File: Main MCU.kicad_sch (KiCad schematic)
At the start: 53 parts, among them J1 F407 SWD, J2 GPIO, J3 Conn_01x02_Pin, SW1 SW_Push, SW2 SW_Push, SW3 SW_Push, SW4 SW_Push, U1 STM32F407VGTx, U2 MCP1825S-3302E/EB

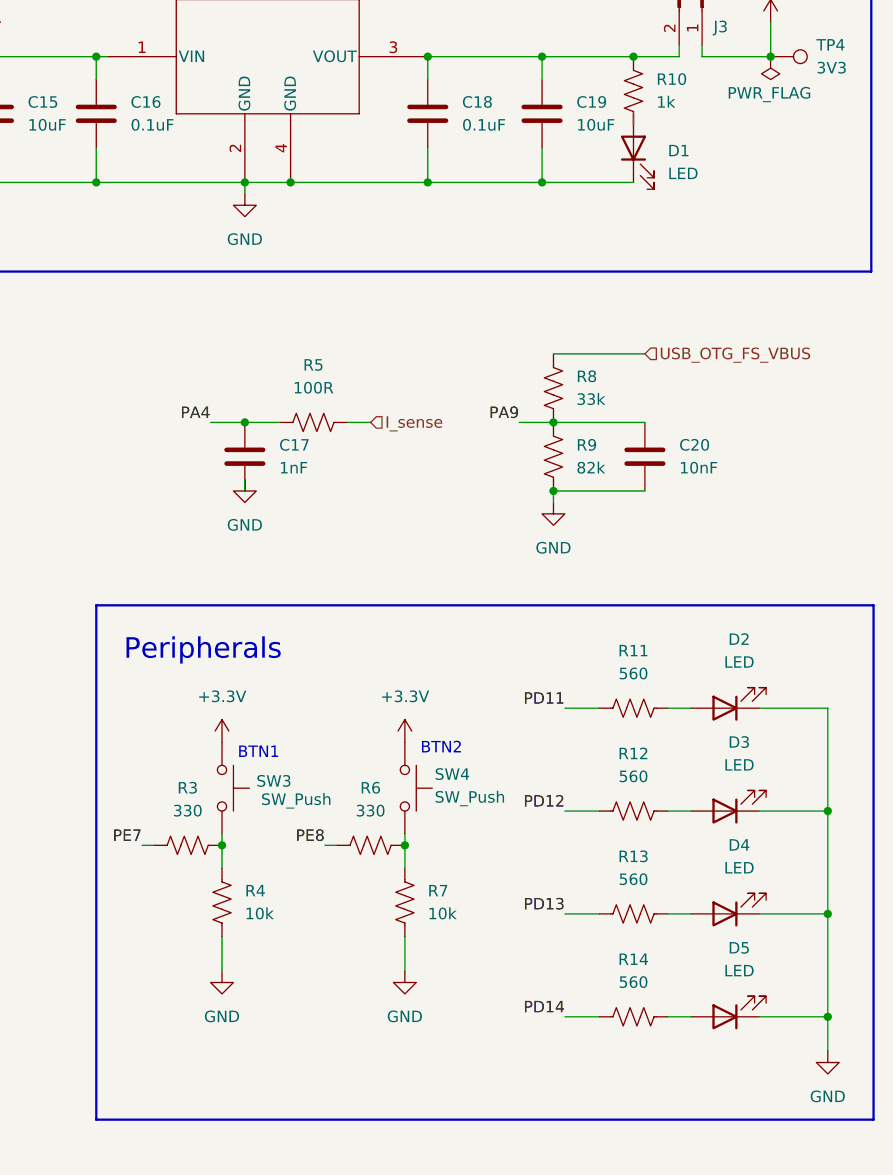
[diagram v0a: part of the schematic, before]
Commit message: MPNs updated
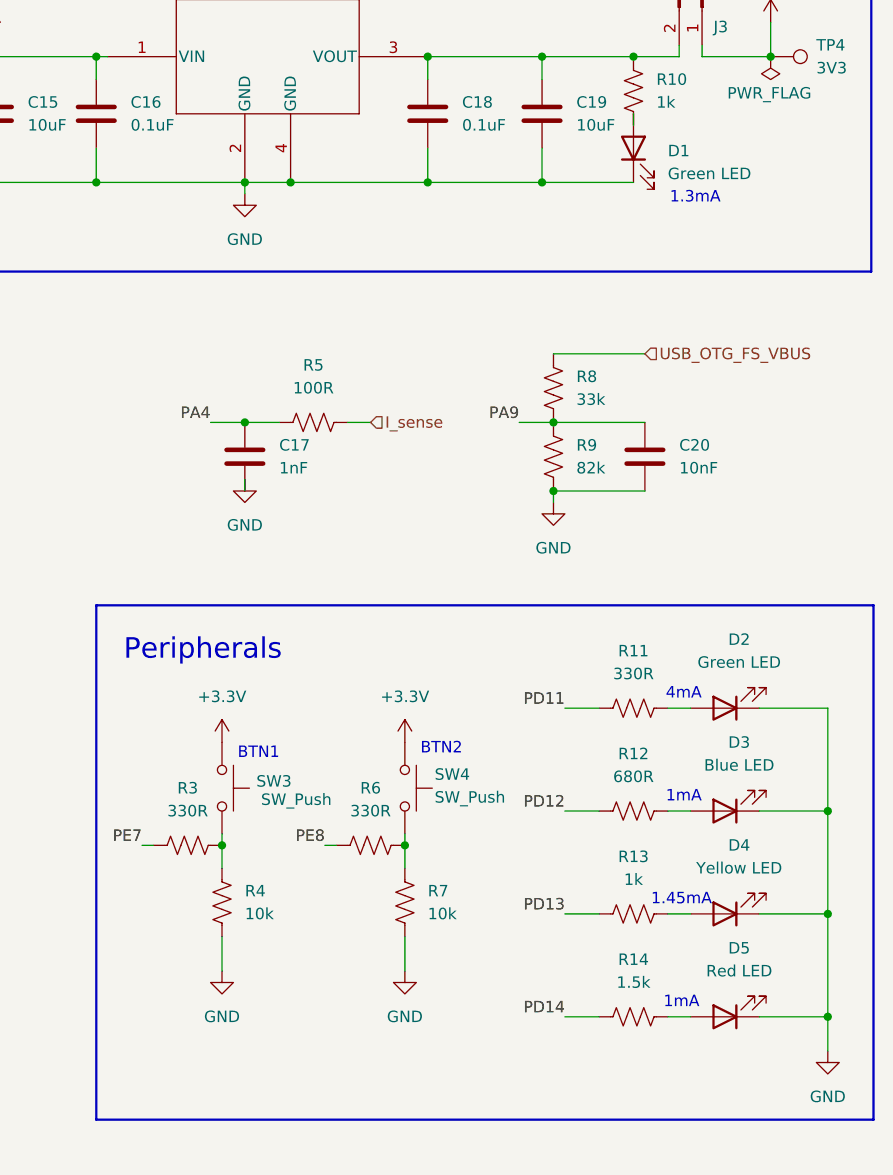
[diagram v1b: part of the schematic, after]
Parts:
- C15, C19: MPN (none) -> CL21B106KOQNNNE
- C17: MPN (none) -> GRM188R72A102KA01D
- C2, C5: MPN (none) -> CL10B225KP8NNNC
- D1, D2: value LED -> Green LED; MPN (none) -> APT2012CGCK
- D3: value LED -> Blue LED; MPN (none) -> APT2012LVBC/D
- D4: value LED -> Yellow LED; MPN (none) -> APT2012SYCK
- D5: value LED -> Red LED; MPN (none) -> APT2012SURCK
- R1, R2, R4, R7: MPN (none) -> RC0603FR-0710KL
- R10: MPN (none) -> RC0603FR-071KL
- R11: value 560 -> 330R; MPN (none) -> RC0603FR-07330RL
- R12: value 560 -> 680R; MPN (none) -> RC0603FR-07680RL
- R13: value 560 -> 1k; MPN (none) -> RC0603FR-071KL
- R14: value 560 -> 1.5k; MPN (none) -> RC0603FR-071K5L
- R3, R6: value 330 -> 330R; MPN (none) -> RC0603FR-07330RL
- R5: MPN (none) -> RC0603FR-07100RL
- R8: MPN (none) -> RC0603FR-0733KL
- R9: MPN (none) -> RC0603FR-0782KL
- U1: MPN STM32F407VGTx -> STM32F407VGT6
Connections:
- net PD11: now also R11.1; no longer R11.2
- net PD12: now also R12.1; no longer R12.2
- net at D3.2 (A): now also R12.2; no longer R12.1
- net at D2.2 (A): now also R11.2; no longer R11.1
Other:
- note added: "1.3mA"
- note added: "1.45mA"
- note added: "1mA"
- note added: "4mA"

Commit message: Layout placement
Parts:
- removed J2: GPIO, Connector_PinHeader_2.54mm:PinHeader_2x09_P2.54mm_Vertical, symbol Connector_Generic:Conn_02x09_Top_Bottom
- added J2: GPIO, Connector_PinHeader_2.54mm:PinHeader_2x09_P2.54mm_Vertical, symbol Connector_Generic:Conn_02x09_Odd_Even
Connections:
- net +3.3V: now also J2.5 (Pin_5), J2.6 (Pin_6)
- net +5V: now also J2.3 (Pin_3), J2.4 (Pin_4)
- net GND: now also J2.1 (Pin_1), J2.2 (Pin_2)
- net PA0: now also J2.17 (Pin_17)
- net PA3: now also J2.10 (Pin_10)
- net PA5: now also J2.11 (Pin_11)
- net PA6: now also J2.15 (Pin_15)
- net PA8: now also J2.7 (Pin_7)
- net PB1: now also J2.12 (Pin_12)
- net PB5: now also J2.13 (Pin_13)
- net PC11: now also J2.18 (Pin_18)
- net PC9: now also J2.9 (Pin_9)
- net PD15: now also J2.16 (Pin_16)
- net PE14: now also J2.14 (Pin_14)
- net RESET: now also J2.8 (Pin_8)
- net RX: now reaches U1.86 (PD5)
- net TX: now reaches U1.87 (PD6)
- no-connect marks 36 -> 34
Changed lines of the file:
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@@
 	(text "1.3mA"
 		(exclude_from_sim no)
-		(at 260.858 56.388 0)
+		(at 252.476 56.642 0)
 		(effects
 			(font
@@
 	)
 	(no_connect
-		(at 105.41 135.89)
-	)
-	(no_connect
 		(at 156.21 146.05)
 	)
 	(no_connect
-		(at 105.41 133.35)
-	)
-	(no_connect
 		(at 105.41 102.87)
 	)
@@
 	(wire
 		(pts
+			(xy 93.98 133.35) (xy 105.41 133.35)
+		)
+		(stroke
+			(width 0)
+			(type default)
+		)
+	)
+	(wire
+		(pts
 			(xy 123.19 189.23) (xy 125.73 189.23)
 		)
@@
 	(wire
 		(pts
+			(xy 93.98 135.89) (xy 105.41 135.89)
+		)
+		(stroke
+			(width 0)
+			(type default)
+		)
+	)
+	(wire
+		(pts
 			(xy 127 43.18) (xy 127 44.45)
 		)
@@
 		)
 	)
+	(hierarchical_label "RX"
+		(shape bidirectional)
+		(at 93.98 133.35 180)
+		(effects
+			(font
+				(size 1.27 1.27)
+			)
+			(justify right)
+		)
+	)
 	(hierarchical_label "TX_D1"
 		(shape output)
@@
 		)
 	)
+	(hierarchical_label "TX"
+		(shape bidirectional)
+		(at 93.98 135.89 180)
+		(effects
+			(font
+				(size 1.27 1.27)
+			)
+			(justify right)
+		)
+	)
 	(hierarchical_label "T_SWO"
 		(shape bidirectional)
@@
 	)
 	(symbol
-		(lib_id "Connector_Generic:Conn_02x09_Top_Bottom")
-		(at 44.45 115.57 0)
-		(unit 1)
-		(exclude_from_sim no)
-		(in_bom yes)
-		(on_board yes)
-		(dnp no)
-		(property "Reference" "J2"
-			(at 45.72 100.838 0)
-			(effects
-				(font
-					(size 1.27 1.27)
-				)
-			)
-		)
-		(property "Value" "GPIO"
-			(at 45.72 102.87 0)
-			(effects
-				(font
-					(size 1.27 1.27)
-				)
-			)
-		)
-		(property "Footprint" "Connector_PinHeader_2.54mm:PinHeader_2x09_P2.54mm_Vertical"
-			(at 44.45 115.57 0)
-			(effects
-				(font
-					(size 1.27 1.27)
-				)
-				(hide yes)
-			)
-		)
-		(property "Datasheet" "~"
-			(at 44.45 115.57 0)
-			(effects
-				(font
-					(size 1.27 1.27)
-				)
-				(hide yes)
-			)
-		)
-		(property "Description" "Generic connector, double row, 02x09, top/bottom pin numbering scheme (row 1: 1...pins_per_row, row2: pins_per_row+1 ... num_pins), script generated (kicad-library-utils/schlib/autogen/connector/)"
-			(at 44.45 115.57 0)
-			(effects
-				(font
-					(size 1.27 1.27)
-				)
-				(hide yes)
-			)
-		)
-		(property "Manufacturer_Part_Number" ""
-			(at 44.45 115.57 0)
-			(effects
-				(font
-					(size 1.27 1.27)
-				)
-				(hide yes)
-			)
-		)
-		(pin "8"
-		)
-		(pin "12"
-		)
-		(pin "17"
-		)
-		(pin "18"
-		)
-		(pin "16"
-		)
-		(pin "4"
-		)
-		(pin "3"
-		)
-		(pin "11"
-		)
-		(pin "13"
-		)
-		(pin "5"
-		)
-		(pin "2"
-		)
-		(pin "6"
-		)
-		(pin "9"
-		)
-		(pin "1"
-		)
-		(pin "7"
-		)
-		(pin "10"
-		)
-		(pin "14"
-		)
-		(pin "15"
-		)
-		(instances
-			(project "STM32 Microcontroller Board"
-				(path "/c703575f-b97a-4282-ae81-d5777b8a5a01/a27108a6-f904-49cb-857a-5db6dcb2e7fa"
-					(reference "J2")
-					(unit 1)
-				)
-			)
-		)
-	)
-	(symbol
 		(lib_id "power:GND")
 		(at 208.28 142.24 0)
@@
 		(on_board yes)
 		(dnp no)
-		(fields_autoplaced yes)
 		(property "Reference" "D3"
-			(at 265.7475 116.84 0)
+			(at 265.684 116.84 0)
 			(effects
 				(font
@@
 		)
 		(property "Value" "Blue LED"
-			(at 265.7475 119.38 0)
+			(at 265.684 118.872 0)
 			(effects
 				(font
@@
 		)
 		(property "MPN" "APT2012LVBC/D"
-			(at 264.16 124.46 0)
+			(at 265.684 120.904 0)
 			(effects
 				(font
-					(size 1.27 1.27)
+					(size 0.889 0.889)
 				)
-				(hide yes)
 			)
 		)
@@
 		(on_board yes)
 		(dnp no)
-		(fields_autoplaced yes)
 		(property "Reference" "D1"
 			(at 257.81 51.1174 90)
@@
 		)
 		(property "MPN" "APT2012CGCK"
-			(at 254 50.8 0)
+			(at 262.636 56.134 90)
 			(effects
 				(font
-					(size 1.27 1.27)
+					(size 0.889 0.889)
 				)
-				(hide yes)
 			)
 		)
@@
 		(on_board yes)
 		(dnp no)
-		(fields_autoplaced yes)
 		(property "Reference" "D5"
-			(at 265.7475 139.7 0)
+			(at 265.7475 139.192 0)
 			(effects
 				(font
@@
 		)
 		(property "Value" "Red LED"
-			(at 265.7475 142.24 0)
+			(at 265.684 141.478 0)
 			(effects
 				(font
@@
 		)
 		(property "MPN" "APT2012SURCK"
-			(at 264.16 147.32 0)
+			(at 264.922 143.51 0)
 			(effects
 				(font
-					(size 1.27 1.27)
+					(size 0.889 0.889)
 				)
-				(hide yes)
 			)
 		)
@@
 	)
 	(symbol
+		(lib_id "Connector_Generic:Conn_02x09_Odd_Even")
+		(at 44.45 115.57 0)
+		(unit 1)
+		(exclude_from_sim no)
+		(in_bom yes)
+		(on_board yes)
+		(dnp no)
+		(fields_autoplaced yes)
+		(property "Reference" "J2"
+			(at 45.72 99.06 0)
+			(effects
+				(font
+					(size 1.27 1.27)
+				)
+			)
+		)
+		(property "Value" "GPIO"
+			(at 45.72 101.6 0)
+			(effects
+				(font
+					(size 1.27 1.27)
+				)
+			)
+		)
+		(property "Footprint" "Connector_PinHeader_2.54mm:PinHeader_2x09_P2.54mm_Vertical"
+			(at 44.45 115.57 0)
+			(effects
+				(font
+					(size 1.27 1.27)
+				)
+				(hide yes)
+			)
+		)
+		(property "Datasheet" "~"
+			(at 44.45 115.57 0)
+			(effects
+				(font
+					(size 1.27 1.27)
+				)
+				(hide yes)
+			)
+		)
+		(property "Description" "Generic connector, double row, 02x09, odd/even pin numbering scheme (row 1 odd numbers, row 2 even numbers), script generated (kicad-library-utils/schlib/autogen/connector/)"
+			(at 44.45 115.57 0)
+			(effects
+				(font
+					(size 1.27 1.27)
+				)
+				(hide yes)
+			)
+		)
+		(pin "9"
+		)
+		(pin "15"
+		)
+		(pin "3"
+		)
+		(pin "1"
+		)
+		(pin "11"
+		)
+		(pin "14"
+		)
+		(pin "4"
+		)
+		(pin "8"
+		)
+		(pin "5"
+		)
+		(pin "7"
+		)
+		(pin "13"
+		)
+		(pin "10"
+		)
+		(pin "12"
+		)
+		(pin "6"
+		)
+		(pin "2"
+		)
+		(pin "18"
+		)
+		(pin "17"
+		)
+		(pin "16"
+		)
+		(instances
+			(project ""
+				(path "/c703575f-b97a-4282-ae81-d5777b8a5a01/a27108a6-f904-49cb-857a-5db6dcb2e7fa"
+					(reference "J2")
+					(unit 1)
+				)
+			)
+		)
+	)
+	(symbol
 		(lib_id "Device:C")
 		(at 100.33 41.91 0)
@@
 		(on_board yes)
 		(dnp no)
-		(fields_autoplaced yes)
 		(property "Reference" "FB1"
-			(at 86.36 25.4507 0)
+			(at 86.36 24.9427 0)
 			(effects
 				(font
@@
 		)
 		(property "Value" "FerriteBead"
-			(at 86.36 27.9907 0)
+			(at 86.36 27.4827 0)
 			(effects
 				(font
@@
 		)
 		(property "MPN" "MPZ1608S601ATA00"
-			(at 82.55 26.67 0)
+			(at 91.694 29.718 0)
 			(effects
 				(font
-					(size 1.27 1.27)
+					(size 0.889 0.889)
 				)
-				(hide yes)
 			)
 		)
@@
 		(on_board yes)
 		(dnp no)
-		(fields_autoplaced yes)
 		(property "Reference" "D2"
-			(at 265.7475 105.41 0)
+			(at 265.684 105.41 0)
 			(effects
 				(font
@@
 		)
 		(property "Value" "Green LED"
-			(at 265.7475 107.95 0)
+			(at 265.684 107.188 0)
 			(effects
 				(font
@@
 		)
 		(property "MPN" "APT2012CGCK"
-			(at 264.16 113.03 0)
+			(at 265.684 109.22 0)
 			(effects
 				(font
-					(size 1.27 1.27)
+					(size 0.889 0.889)
 				)
-				(hide yes)
 			)
 		)
@@
 		(on_board yes)
 		(dnp no)
-		(fields_autoplaced yes)
 		(property "Reference" "D4"
-			(at 265.7475 128.27 0)
+			(at 265.684 128.016 0)
 			(effects
 				(font
@@
 		)
 		(property "Value" "Yellow LED"
-			(at 265.7475 130.81 0)
+			(at 265.684 130.048 0)
 			(effects
 				(font
@@
 		)
 		(property "MPN" "APT2012SYCK"
-			(at 264.16 135.89 0)
+			(at 265.43 132.334 0)
 			(effects
 				(font
-					(size 1.27 1.27)
+					(size 0.889 0.889)
 				)
-				(hide yes)
 			)
 		)

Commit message: Layout Routing
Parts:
- added C17: 0.1uF, Capacitor_SMD:C_0402_1005Metric, symbol Device:C
- added D1: 3.3V, Diode_SMD:D_SOD-323F, symbol Diode:MM3Zxx
- FB1: MPN MPZ1608S601ATA00 -> MPZ1608S601
- renumbered C17 to C18, C18 to C19, C19 to C20, C20 to C21, C7 to C6, C6 to C7, C9 to C8, C8 to C9, D1 to D2, D2 to D3, D3 to D4, D4 to D5, D5 to D6, R11 to R10, R12 to R11, R13 to R12, R14 to R13, R10 to R14
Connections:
- net GND: now also C17.2, D1.2 (A)
- net PC8: now reaches U1.65 (PC8)
- net PC8: now also J2.12 (Pin_12)
- net PB1 renamed V_sense
- net V_sense: now also C17.1, D1.1 (K); no longer J2.12 (Pin_12)
- no-connect marks 34 -> 33
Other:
- moved on the sheet: C10, C11, C12, C13, C14, C15, C16, C18, C19, C20, C21, C7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

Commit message: Review files
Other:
- company: _electronic_projects -> (none)
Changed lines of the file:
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@@
 		(title "DeskNode-F4")
 		(rev "A")
-		(company "_electronic_projects")
-		(comment 1 "Wajahatulla Sharif")
-		(comment 2 "Designed by ")
 	)
 	(rectangle
